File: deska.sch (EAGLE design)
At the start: 17 parts, among them Q1 BC547, Q2 BC547

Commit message: +
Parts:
- UART: device con-wago-508:W237-02P -> con-wago-508:W237-3E
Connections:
- removed net +3V3: BUZZER-2.KL, I2C-2.KL, R1.2, R2.2, R3.2, RELAY-2.KL, TIN-1.KL, TOUT-1.KL, TUT-1.KL, U$1.RAW
- removed net N$8: TIN-2.KL, TOUT-3.KL, TUT-3.KL
- new net +5V: I2C-2.KL, LED-2.KL, R1.2, R2.2, R3.2, RELAY-2.KL, TIN-1.KL, TOUT-1.KL, TUT-1.KL, U$1.RAW
- net GND: now also BUZZER-2.KL, TIN-2.KL, TOUT-3.KL, TUT-3.KL, UART-1.KL; no longer LED-2.KL
- net N$10: now also UART-3.KL; no longer UART-2.KL
- net N$9: now also UART-2.KL; no longer UART-1.KL
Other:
- moved on the sheet: BUZZER-1, BUZZER-2, I2C-1, I2C-2, I2C-3, I2C-4, LED-1, LED-2, Q2, R4, RELAY-2, TIN-2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

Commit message: zmeny
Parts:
- removed I2C: (no value), con-wago-508:W237-04P
- added COMMUNIT: (no value), con-wago-508:W237-02P
- added I2CDISP, I2CHOUR, I2CKEYB, LEDDISP: (no value), con-wago-508:W237-04P
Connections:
- new net N$17: COMMUNIT-2.KL, U$1.A0
- new net N$8: COMMUNIT-1.KL, U$1.A1
- net +5V: now also I2CDISP-2.KL, I2CHOUR-2.KL, I2CKEYB-2.KL, LEDDISP-2.KL; no longer I2C-2.KL
- net GND: now also I2CDISP-1.KL, I2CHOUR-1.KL, I2CKEYB-1.KL, LEDDISP-1.KL, TIN-3.KL; no longer I2C-1.KL, TIN-2.KL
- net N$1: now also TIN-2.KL; no longer TIN-3.KL
- net N$11: now also I2CDISP-4.KL, I2CHOUR-4.KL, I2CKEYB-4.KL, LEDDISP-4.KL; no longer I2C-4.KL
- net N$12: now also I2CDISP-3.KL, I2CHOUR-3.KL, I2CKEYB-3.KL, LEDDISP-3.KL; no longer I2C-3.KL
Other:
- moved on the sheet: BUZZER-1, BUZZER-2, Q1, R6

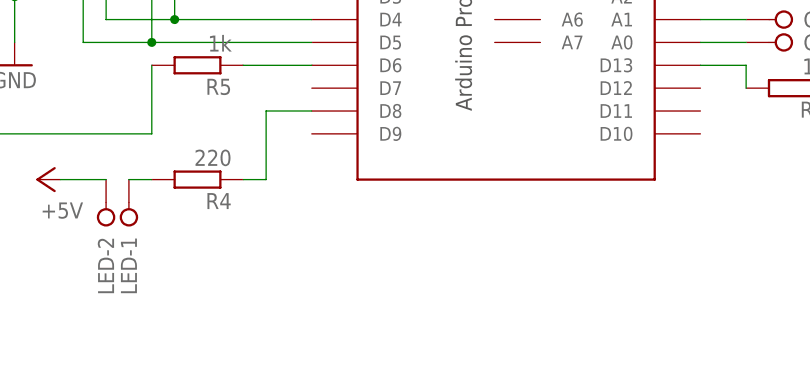
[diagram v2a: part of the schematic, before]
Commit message: uprava desky, prida konektor pro napajeni
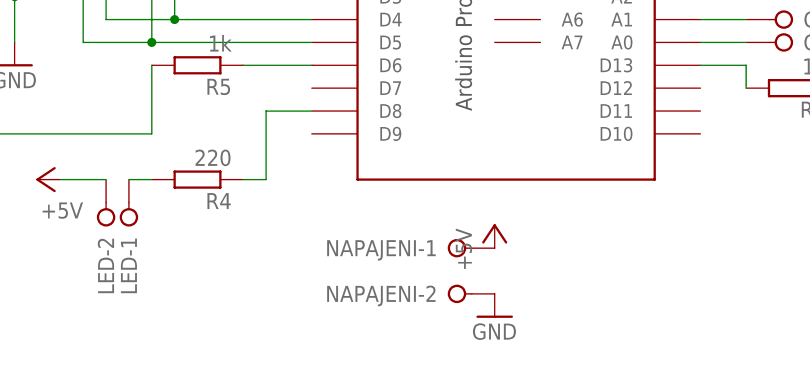
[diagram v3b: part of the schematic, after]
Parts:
- added NAPAJENI: (no value), con-wago-508:W237-02P
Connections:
- net +5V: now also NAPAJENI-1.KL
- net GND: now also NAPAJENI-2.KL
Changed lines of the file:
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@@
 <part name="COMMUNIT" library="con-wago-508" deviceset="W237-02P" device=""/>
 <part name="LEDDISP" library="con-wago-508" deviceset="W237-04P" device=""/>
+<part name="NAPAJENI" library="con-wago-508" deviceset="W237-02P" device=""/>
+<part name="P+5" library="supply1" deviceset="+5V" device=""/>
+<part name="GND6" library="supply1" deviceset="GND" device=""/>
 </parts>
 <sheets>
@@
 <instance part="LEDDISP" gate="-3" x="137.16" y="86.36" rot="R270"/>
 <instance part="LEDDISP" gate="-4" x="134.62" y="86.36" rot="R270"/>
+<instance part="NAPAJENI" gate="-1" x="48.26" y="30.48"/>
+<instance part="NAPAJENI" gate="-2" x="48.26" y="25.4"/>
+<instance part="P+5" gate="1" x="53.34" y="33.02"/>
+<instance part="GND6" gate="1" x="53.34" y="22.86"/>
 </instances>
 <busses>
@@
 <wire x1="0" y1="88.9" x2="-2.54" y2="88.9" width="0.1524" layer="91"/>
 </segment>
+<segment>
+<pinref part="NAPAJENI" gate="-2" pin="KL"/>
+<pinref part="GND6" gate="1" pin="GND"/>
+</segment>
 </net>
 <net name="N$5" class="0">
@@
 <junction x="124.46" y="71.12"/>
 </segment>
-</net>
+<segment>
+<pinref part="NAPAJENI" gate="-1" pin="KL"/>
+<pinref part="P+5" gate="1" pin="+5V"/>
+</segment>
+</net>

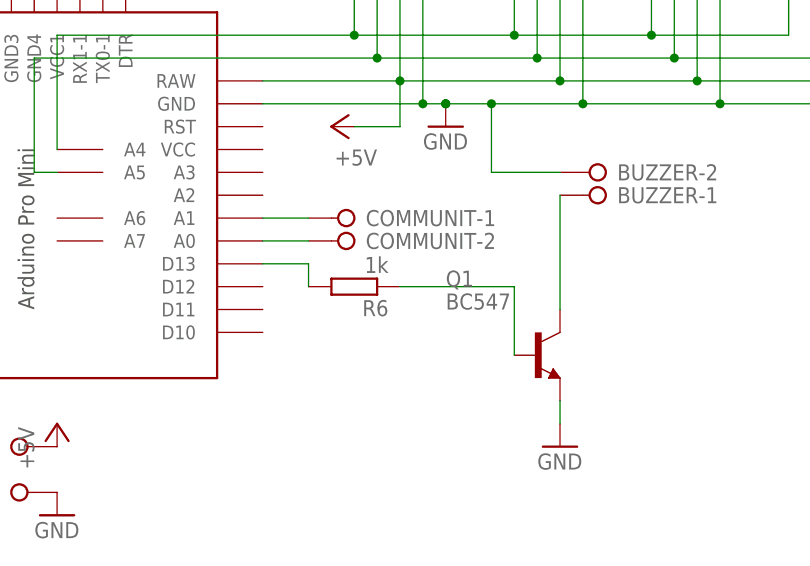
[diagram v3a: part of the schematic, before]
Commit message: +upraveny DPS DPS objednany 27.4.2016
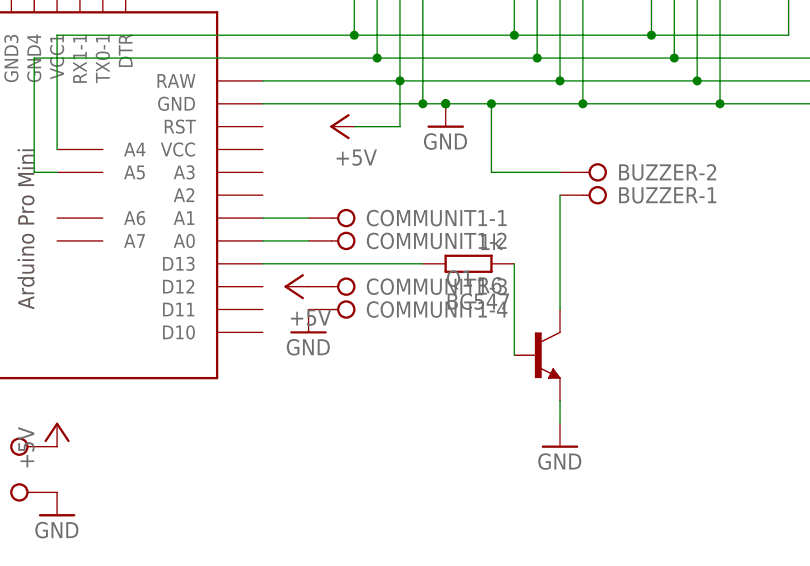
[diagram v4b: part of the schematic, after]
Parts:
- removed COMMUNIT: (no value), con-wago-508:W237-02P
- added COMMUNIT1: (no value), con-wago-508:W237-04P
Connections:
- net +5V: now also COMMUNIT1-3.KL
- net GND: now also COMMUNIT1-4.KL
- net N$17: now also COMMUNIT1-2.KL; no longer COMMUNIT-2.KL
- net N$8: now also COMMUNIT1-1.KL; no longer COMMUNIT-1.KL
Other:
- moved on the sheet: R6
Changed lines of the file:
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@@
 <part name="I2CKEYB" library="con-wago-508" deviceset="W237-04P" device=""/>
 <part name="I2CHOUR" library="con-wago-508" deviceset="W237-04P" device=""/>
-<part name="COMMUNIT" library="con-wago-508" deviceset="W237-02P" device=""/>
 <part name="LEDDISP" library="con-wago-508" deviceset="W237-04P" device=""/>
 <part name="NAPAJENI" library="con-wago-508" deviceset="W237-02P" device=""/>
 <part name="P+5" library="supply1" deviceset="+5V" device=""/>
 <part name="GND6" library="supply1" deviceset="GND" device=""/>
+<part name="P+6" library="supply1" deviceset="+5V" device=""/>
+<part name="GND7" library="supply1" deviceset="GND" device=""/>
+<part name="COMMUNIT1" library="con-wago-508" deviceset="W237-04P" device=""/>
 </parts>
 <sheets>
@@
 <instance part="Q2" gate="G$1" x="-22.86" y="43.18" rot="MR0"/>
 <instance part="R5" gate="G$1" x="20.32" y="50.8" rot="R180"/>
-<instance part="R6" gate="G$1" x="86.36" y="48.26" rot="R180"/>
+<instance part="R6" gate="G$1" x="99.06" y="50.8" rot="R180"/>
 <instance part="I2CDISP" gate="-1" x="93.98" y="86.36" rot="R270"/>
 <instance part="I2CDISP" gate="-2" x="91.44" y="86.36" rot="R270"/>
@@
 <instance part="I2CHOUR" gate="-3" x="121.92" y="86.36" rot="R270"/>
 <instance part="I2CHOUR" gate="-4" x="119.38" y="86.36" rot="R270"/>
-<instance part="COMMUNIT" gate="-1" x="86.36" y="55.88" rot="R180"/>
-<instance part="COMMUNIT" gate="-2" x="86.36" y="53.34" rot="R180"/>
 <instance part="LEDDISP" gate="-1" x="142.24" y="86.36" rot="R270"/>
 <instance part="LEDDISP" gate="-2" x="139.7" y="86.36" rot="R270"/>
@@
 <instance part="P+5" gate="1" x="53.34" y="33.02"/>
 <instance part="GND6" gate="1" x="53.34" y="22.86"/>
+<instance part="P+6" gate="1" x="78.74" y="48.26" rot="R90"/>
+<instance part="GND7" gate="1" x="81.28" y="43.18"/>
+<instance part="COMMUNIT1" gate="-1" x="86.36" y="55.88" rot="R180"/>
+<instance part="COMMUNIT1" gate="-2" x="86.36" y="53.34" rot="R180"/>
+<instance part="COMMUNIT1" gate="-3" x="86.36" y="48.26" rot="R180"/>
+<instance part="COMMUNIT1" gate="-4" x="86.36" y="45.72" rot="R180"/>
 </instances>
 <busses>
@@
 <pinref part="GND6" gate="1" pin="GND"/>
 </segment>
+<segment>
+<pinref part="GND7" gate="1" pin="GND"/>
+<pinref part="COMMUNIT1" gate="-4" pin="KL"/>
+</segment>
 </net>
 <net name="N$5" class="0">
@@
 </segment>
 </net>
-<net name="N$7" class="0">
-<segment>
-<pinref part="Q1" gate="G$1" pin="B"/>
-<pinref part="R6" gate="G$1" pin="1"/>
-<wire x1="104.14" y1="40.64" x2="104.14" y2="48.26" width="0.1524" layer="91"/>
-<wire x1="104.14" y1="48.26" x2="91.44" y2="48.26" width="0.1524" layer="91"/>
-</segment>
-</net>
 <net name="N$16" class="0">
 <segment>
 <pinref part="R6" gate="G$1" pin="2"/>
 <pinref part="U$1" gate="G$1" pin="D13"/>
-<wire x1="81.28" y1="48.26" x2="81.28" y2="50.8" width="0.1524" layer="91"/>
-<wire x1="81.28" y1="50.8" x2="76.2" y2="50.8" width="0.1524" layer="91"/>
+<wire x1="93.98" y1="50.8" x2="76.2" y2="50.8" width="0.1524" layer="91"/>
 </segment>
 </net>
@@
 <pinref part="P+5" gate="1" pin="+5V"/>
 </segment>
+<segment>
+<pinref part="P+6" gate="1" pin="+5V"/>
+<pinref part="COMMUNIT1" gate="-3" pin="KL"/>
+</segment>
 </net>
 <net name="N$8" class="0">
 <segment>
-<pinref part="COMMUNIT" gate="-1" pin="KL"/>
 <pinref part="U$1" gate="G$1" pin="A1"/>
 <wire x1="81.28" y1="55.88" x2="76.2" y2="55.88" width="0.1524" layer="91"/>
+<pinref part="COMMUNIT1" gate="-1" pin="KL"/>
 </segment>
 </net>
 <net name="N$17" class="0">
 <segment>
-<pinref part="COMMUNIT" gate="-2" pin="KL"/>
 <pinref part="U$1" gate="G$1" pin="A0"/>
 <wire x1="81.28" y1="53.34" x2="76.2" y2="53.34" width="0.1524" layer="91"/>
-</segment>
-</net>
+<pinref part="COMMUNIT1" gate="-2" pin="KL"/>
+</segment>
+</net>
+<net name="N$7" class="0">
+<segment>
+<pinref part="R6" gate="G$1" pin="1"/>
+<pinref part="Q1" gate="G$1" pin="B"/>
+<wire x1="104.14" y1="50.8" x2="104.14" y2="40.64" width="0.1524" layer="91"/>
+</segment>
+</net>
